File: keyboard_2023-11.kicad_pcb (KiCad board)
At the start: 2 copper layers, 250.8 x 97.9 mm, 77 parts, among them J11 Conn_01x07_Socket, J2 Conn_01x04_Socket, J3 Conn_01x07_Socket, J4 Conn_01x07_Pin, J5 Conn_01x04_Socket, J6 Conn_01x07_Pin, J7 Conn_01x04_Socket, SW1 SW_Push, SW10 SW_Push, SW11 SW_Push, SW12 SW_Push, SW13 SW_Push, SW14 SW_Push, SW15 SW_Push, SW16 SW_Push, SW17 SW_Push, SW18 SW_Push, SW19 SW_Push, SW2 SW_Push, SW20 SW_Push, SW21 SW_Push, SW22 SW_Push, SW23 SW_Push, SW24 SW_Push, SW3 SW_Push, SW4 SW_Push, SW5 SW_Push, SW6 SW_Push, SW7 SW_Push, SW8 SW_Push, SW9 SW_Push, U1 MCP23017_SO, U2 MCP23017_SO

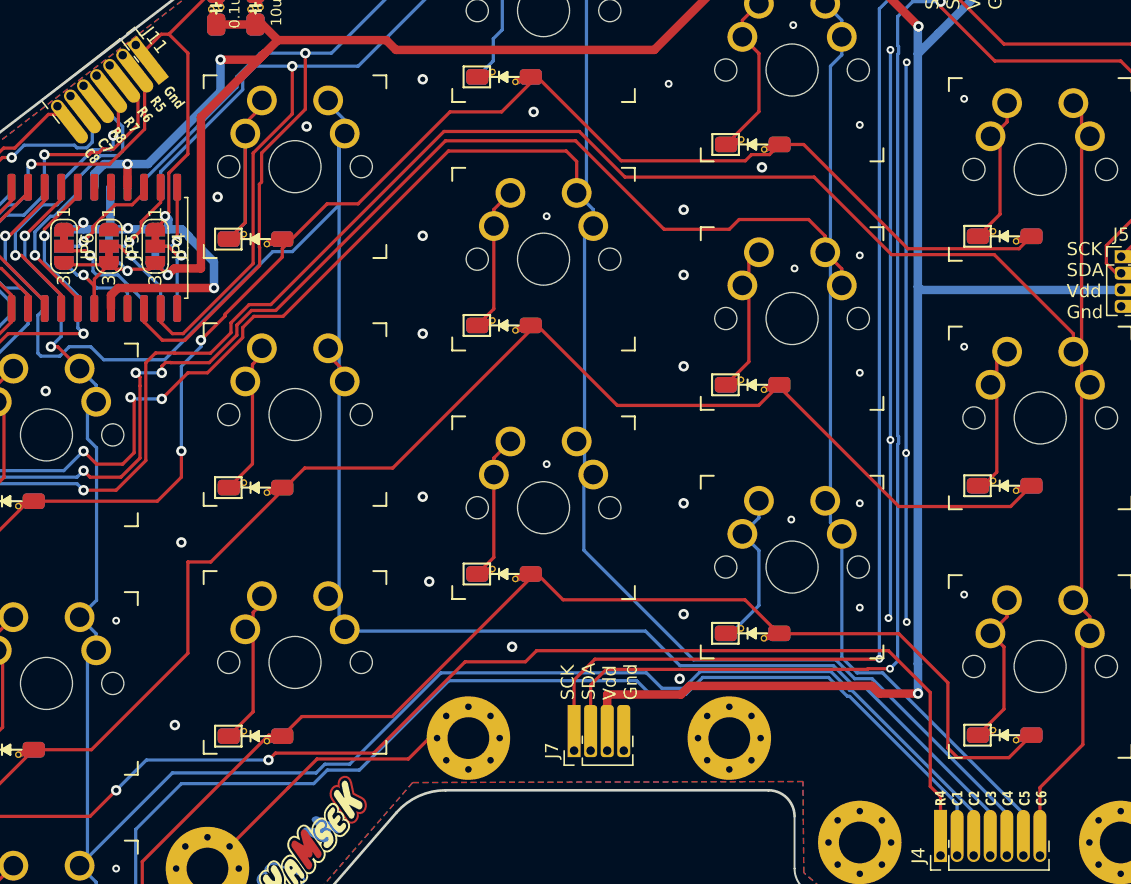
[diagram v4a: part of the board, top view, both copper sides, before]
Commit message: c-numbering from 0 for columns&rows
to better align with the firmware, count from 0 instead of from 1
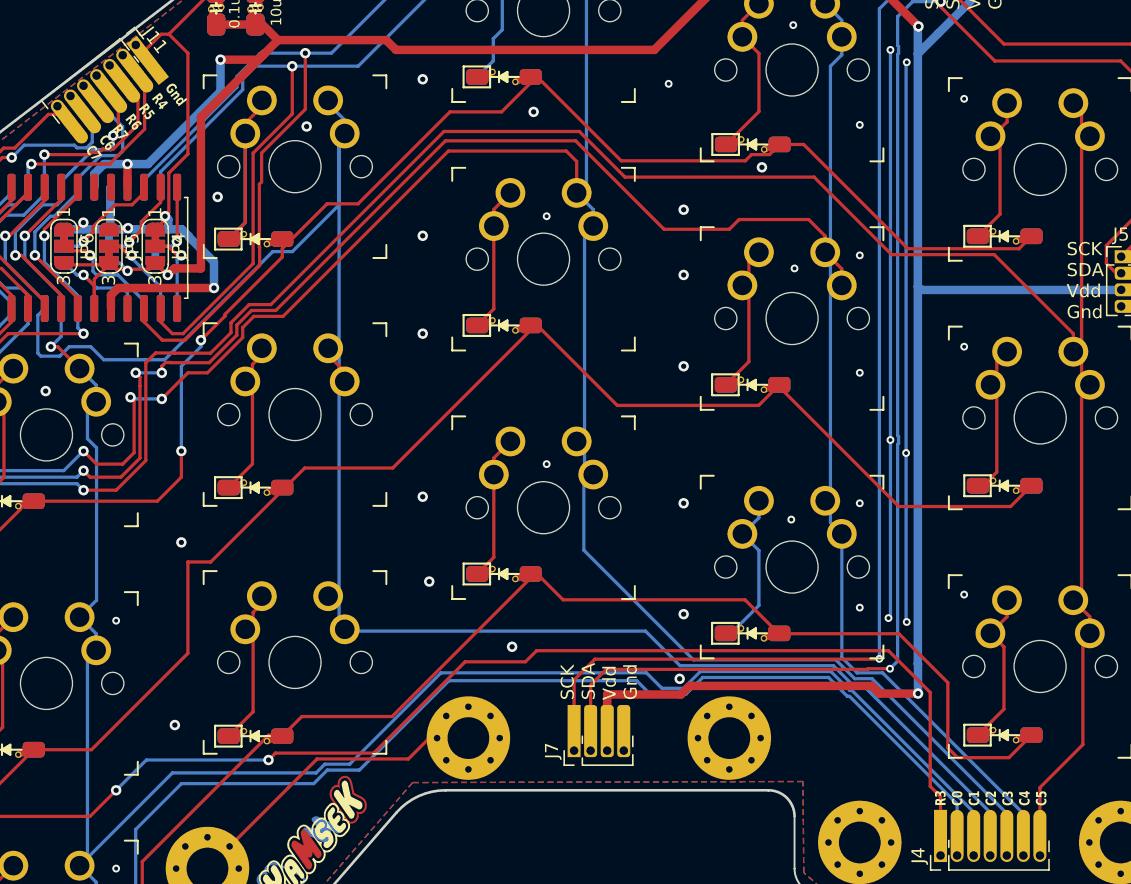
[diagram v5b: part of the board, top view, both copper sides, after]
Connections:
- D1 pad 2: ROW1 -> ROW0
- D10 pad 2: ROW2 -> ROW1
- D11 pad 2: ROW2 -> ROW1
- D12 pad 2: ROW2 -> ROW1
- D13 pad 2: ROW3 -> ROW2
- D14 pad 2: ROW3 -> ROW2
- D15 pad 2: ROW3 -> ROW2
- D16 pad 2: ROW3 -> ROW2
- D17 pad 2: ROW3 -> ROW2
- D18 pad 2: ROW3 -> ROW2
- D2 pad 2: ROW1 -> ROW0
- D3 pad 2: ROW1 -> ROW0
- D4 pad 2: ROW1 -> ROW0
- D5 pad 2: ROW1 -> ROW0
- D6 pad 2: ROW1 -> ROW0
- D7 pad 2: ROW2 -> ROW1
- D8 pad 2: ROW2 -> ROW1
- D9 pad 2: ROW2 -> ROW1
- J11 pad 2: ROW5 -> ROW4
- J11 pad 3: ROW6 -> ROW5
- J11 pad 4: ROW7 -> ROW6
- J11 pad 5: ROW8 -> ROW7
- J11 pad 6: COL7 -> COL6
- J11 pad 7: COL8 -> COL7
- J4 pad 1: ROW4 -> ROW3
- J4 pad 2: COL1 -> COL0
- J4 pad 3: COL2 -> COL1
- J4 pad 4: COL3 -> COL2
- J4 pad 5: COL4 -> COL3
- J4 pad 6: COL5 -> COL4
- J4 pad 7: COL6 -> COL5
- J6 pad 1: ROW5 -> ROW4
- J6 pad 2: COL1 -> COL0
- J6 pad 3: COL2 -> COL1
- J6 pad 4: COL3 -> COL2
- J6 pad 5: COL4 -> COL3
- J6 pad 6: COL5 -> COL4
- J6 pad 7: COL6 -> COL5
- SW1 pad 2: COL1 -> COL0
- SW10 pad 2: COL4 -> COL3
- SW11 pad 2: COL5 -> COL4
- SW12 pad 2: COL6 -> COL5
- SW13 pad 2: COL1 -> COL0
- SW14 pad 2: COL2 -> COL1
- SW15 pad 2: COL3 -> COL2
- SW16 pad 2: COL4 -> COL3
- SW17 pad 2: COL5 -> COL4
- SW18 pad 2: COL6 -> COL5
- SW2 pad 2: COL2 -> COL1
- SW3 pad 2: COL3 -> COL2
- SW4 pad 2: COL4 -> COL3
- SW5 pad 2: COL5 -> COL4
- SW6 pad 2: COL6 -> COL5
- SW7 pad 2: COL1 -> COL0
- SW8 pad 2: COL2 -> COL1
- SW9 pad 2: COL3 -> COL2
- U1 pad 1: ROW1 -> ROW0
- U1 pad 2: ROW2 -> ROW1
- U1 pad 21: COL1 -> COL0
- U1 pad 22: COL2 -> COL1
- U1 pad 23: COL3 -> COL2
- U1 pad 24: COL4 -> COL3
- U1 pad 25: COL5 -> COL4
- U1 pad 26: COL6 -> COL5
- U1 pad 27: COL7 -> COL6
- U1 pad 28: COL8 -> COL7
- U1 pad 3: ROW3 -> ROW2
- U1 pad 4: ROW4 -> ROW3
- U1 pad 5: ROW5 -> ROW4
- U1 pad 6: ROW6 -> ROW5
- U1 pad 7: ROW7 -> ROW6
- U1 pad 8: ROW8 -> ROW7
- U2 pad 1: ROW1 -> ROW0
- U2 pad 2: ROW2 -> ROW1
- U2 pad 21: COL1 -> COL0
- U2 pad 22: COL2 -> COL1
- U2 pad 23: COL3 -> COL2
- U2 pad 24: COL4 -> COL3
- U2 pad 25: COL5 -> COL4
- U2 pad 26: COL6 -> COL5
- U2 pad 27: COL7 -> COL6
- U2 pad 28: COL8 -> COL7
- U2 pad 3: ROW3 -> ROW2
- U2 pad 4: ROW4 -> ROW3
- U2 pad 5: ROW5 -> ROW4
- U2 pad 6: ROW6 -> ROW5
- U2 pad 7: ROW7 -> ROW6
- U2 pad 8: ROW8 -> ROW7
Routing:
- net COL0: track 0.00 -> 191.0 mm, vias 0 -> 3
- net COL6: track 201.9 -> 32.7 mm
- net ROW0: track 0.00 -> 163.5 mm, vias 0 -> 5
- net ROW4: track 155.7 -> 33.6 mm, vias 3 -> 2
- net ROW3: track 211.3 -> 155.7 mm, vias 1 -> 3
- net COL1: track 191.0 -> 145.1 mm, vias 3 -> 2
- net COL8: track 30.9 -> 0.00 mm, vias 1 -> 0
- net COL3: track 153.6 -> 184.1 mm, vias 1 -> 4
- net ROW1: track 163.5 -> 189.2 mm, vias 5 -> 3
- net ROW8: track 22.6 -> 0.00 mm, vias 1 -> 0
- net ROW2: track 189.2 -> 211.3 mm, vias 3 -> 1
- net COL4: track 184.1 -> 194.6 mm
- net COL2: track 145.1 -> 153.6 mm, vias 2 -> 1
- net COL5: track 194.6 -> 201.9 mm, vias 4 -> 2
- net ROW5: track 33.6 -> 28.9 mm
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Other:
- board text added: "Gnd R4 R5 R6 R7 C6 C7"
- board text added: "R3 C0 C1 C2 C3 C4 C5"
- board text removed: "Gnd R5 R6 R7 R8 C7 C8"
- board text removed: "R4 C1 C2 C3 C4 C5 C6"
